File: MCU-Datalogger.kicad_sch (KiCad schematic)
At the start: 0 parts

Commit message: Added symbols into the schematics
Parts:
- added BT1: Battery, symbol Device:Battery
- added C1, C2, C3, C4: C, symbol Device:C
- added C5: C_Polarized, symbol Device:C_Polarized
- added D1, D2: LED, symbol Device:LED
- added H1, H2, H3, H4: MountingHole, symbol Mechanical:MountingHole
- added R1, R2, R3, R4, R5, R6, R7: R, symbol Device:R
- added U1, U2: 24LC1025, symbol Memory_EEPROM:24LC1025
- added U3: DS1337S_, DS1337S_:SOIC127P600X175-8N, symbol DS1337S:DS1337S_
- added U4: ATMEGA328PB-AU, ATMEGA328PB-AU:QFP80P900X900X120-32N, symbol ATMEGA328P-AU:ATMEGA328PB-AU
- added Y1, Y2: Crystal, symbol Device:Crystal
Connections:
- new net GND: U4.21 (GND), U4.5 (GND)
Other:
- added sheet Connectors (Connectors.kicad_sch)
- company: (none) -> Foxhill Labs
- title: (none) -> ${project_name}

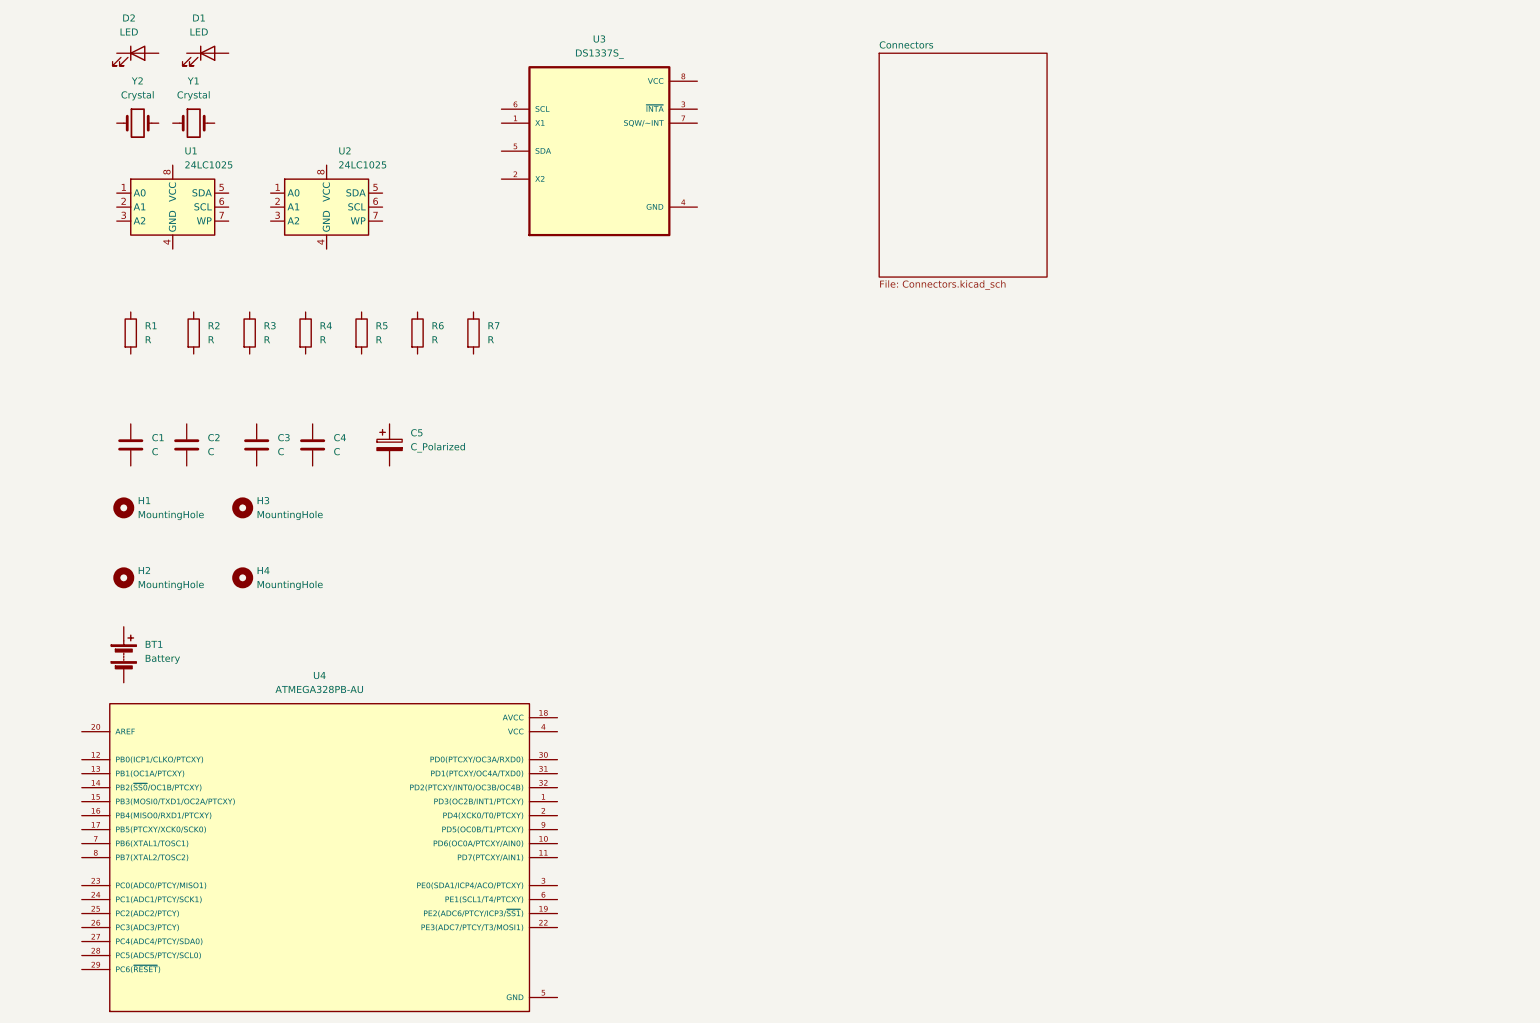
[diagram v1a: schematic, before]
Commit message: Wiring Completion
Wiring completed and the symbols have been rearranged, the footprints were added for all of the symbols. Connector hierarchical sheet added to the project.
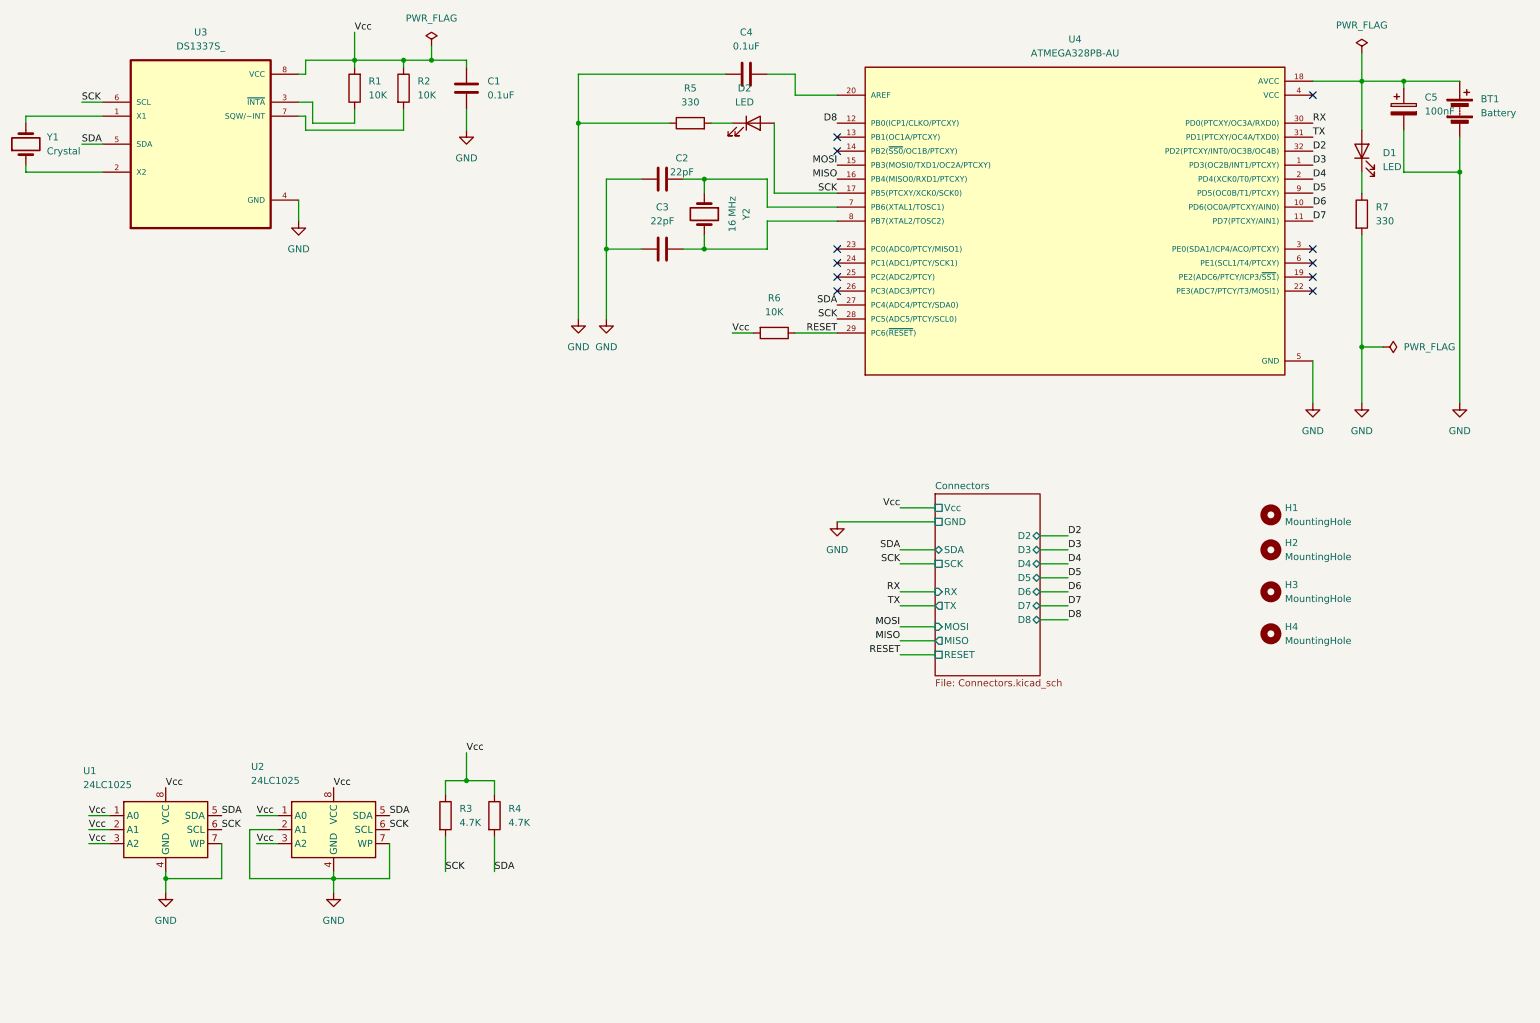
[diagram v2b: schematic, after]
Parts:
- BT1: footprint (none) -> Connector_PinHeader_2.54mm:PinHeader_1x02_P2.54mm_Vertical
- C1, C4: value C -> 0.1uF; footprint (none) -> Capacitor_SMD:C_0805_2012Metric
- C2, C3: value C -> 22pF; footprint (none) -> Capacitor_SMD:C_0805_2012Metric
- C5: value C_Polarized -> 100nF; footprint (none) -> Capacitor_SMD:C_0805_2012Metric
- D1, D2: footprint (none) -> LED_SMD:LED_0805_2012Metric
- H1, H2, H3, H4: footprint (none) -> MountingHole:MountingHole_2.1mm
- R1, R2, R6: value R -> 10K; footprint (none) -> Resistor_SMD:R_0805_2012Metric
- R3, R4: value R -> 4.7K; footprint (none) -> Resistor_SMD:R_0805_2012Metric
- R5, R7: value R -> 330; footprint (none) -> Resistor_SMD:R_0805_2012Metric
- U1, U2: footprint (none) -> Package_SO:SOIC-8_5.3x5.3mm_P1.27mm
- U3: footprint DS1337S_:SOIC127P600X175-8N -> DS1337S:SOIC127P600X175-8N
- U4: footprint ATMEGA328PB-AU:QFP80P900X900X120-32N -> ATMEGA328P-AU:QFP80P900X900X120-32N
- Y1: footprint (none) -> Crystal:Crystal_SMD_5032-2Pin_5.0x3.2mm_HandSoldering
- Y2: value Crystal -> 16 MHz; footprint (none) -> Crystal:Crystal_SMD_5032-2Pin_5.0x3.2mm_HandSoldering
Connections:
- net GND: now also BT1.2 (-), C1.2, C2.1, C3.1, C4.1, C5.2, R5.1, R7.2, U1.4 (GND), U1.7 (WP), U2.2 (A1), U2.4 (GND), U2.7 (WP), U3.4 (GND)
- net at Y1.1: now also U3.2 (X2)
- net at Y1.2: now also U3.1 (X1)
- net Vcc: now reaches R2.1
- net Vcc: now also C1.1, R1.2, R3.1, R4.1, R6.2, U1.1 (A0), U1.2 (A1), U1.3 (A2), U1.8 (VCC), U2.1 (A0), U2.3 (A2), U2.8 (VCC), U3.8 (VCC)
- net at R2.2: now also U3.7 (SQW/~INT)
- net at R7.1: now also D1.1 (K)
- net SDA: now reaches U1.5 (SDA)
- net SDA: now also R4.2, U2.5 (SDA), U3.5 (SDA), U4.27 (PC4(ADC4/PTCY/SDA0))
- net SCK: now reaches U1.6 (SCL)
- net SCK: now also D2.2 (A), R3.2, U2.6 (SCL), U3.6 (SCL), U4.17 (PB5(PTCXY/XCK0/SCK0)), U4.28 (PC5(ADC5/PTCY/SCL0))
- net at C2.2: now also U4.7 (PB6(XTAL1/TOSC1)), Y2.1
- net at D1.2 (A): now also BT1.1 (+), C5.1, U4.18 (AVCC)
- net at U3.3 (~{INTA}): now also R1.1
- net at C3.2: now also U4.8 (PB7(XTAL2/TOSC2)), Y2.2
- net D3: now reaches U4.1 (PD3(OC2B/INT1/PTCXY))
- net D6: now reaches U4.10 (PD6(OC0A/PTCXY/AIN0))
- net D7: now reaches U4.11 (PD7(PTCXY/AIN1))
- net D8: now reaches U4.12 (PB0(ICP1/CLKO/PTCXY))
- net MOSI: now reaches U4.15 (PB3(MOSI0/TXD1/OC2A/PTCXY))
- net MISO: now reaches U4.16 (PB4(MISO0/RXD1/PTCXY))
- net D4: now reaches U4.2 (PD4(XCK0/T0/PTCXY))
- net at U4.20 (AREF): now also C4.2
- net RESET: now reaches U4.29 (PC6(~{RESET}))
- net RESET: now also R6.1
- net RX: now reaches U4.30 (PD0(PTCXY/OC3A/RXD0))
- net TX: now reaches U4.31 (PD1(PTCXY/OC4A/TXD0))
- net D2: now reaches U4.32 (PD2(PTCXY/INT0/OC3B/OC4B))
- net D5: now reaches U4.9 (PD5(OC0B/T1/PTCXY))
- net at D2.1 (K): now also R5.2
- no-connect marks 0 -> 11
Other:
- sheet Connectors ports: added D2, D3, D4, D5, D6, D7, D8, GND, MISO, MOSI, RESET, RX, SCK, SDA, TX, Vcc; removed none
- moved on the sheet: BT1, C1, C2, C3, C4, C5, D1, D2, H1, H2, H3, H4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

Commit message: Comments
Completed the comments for the schematics
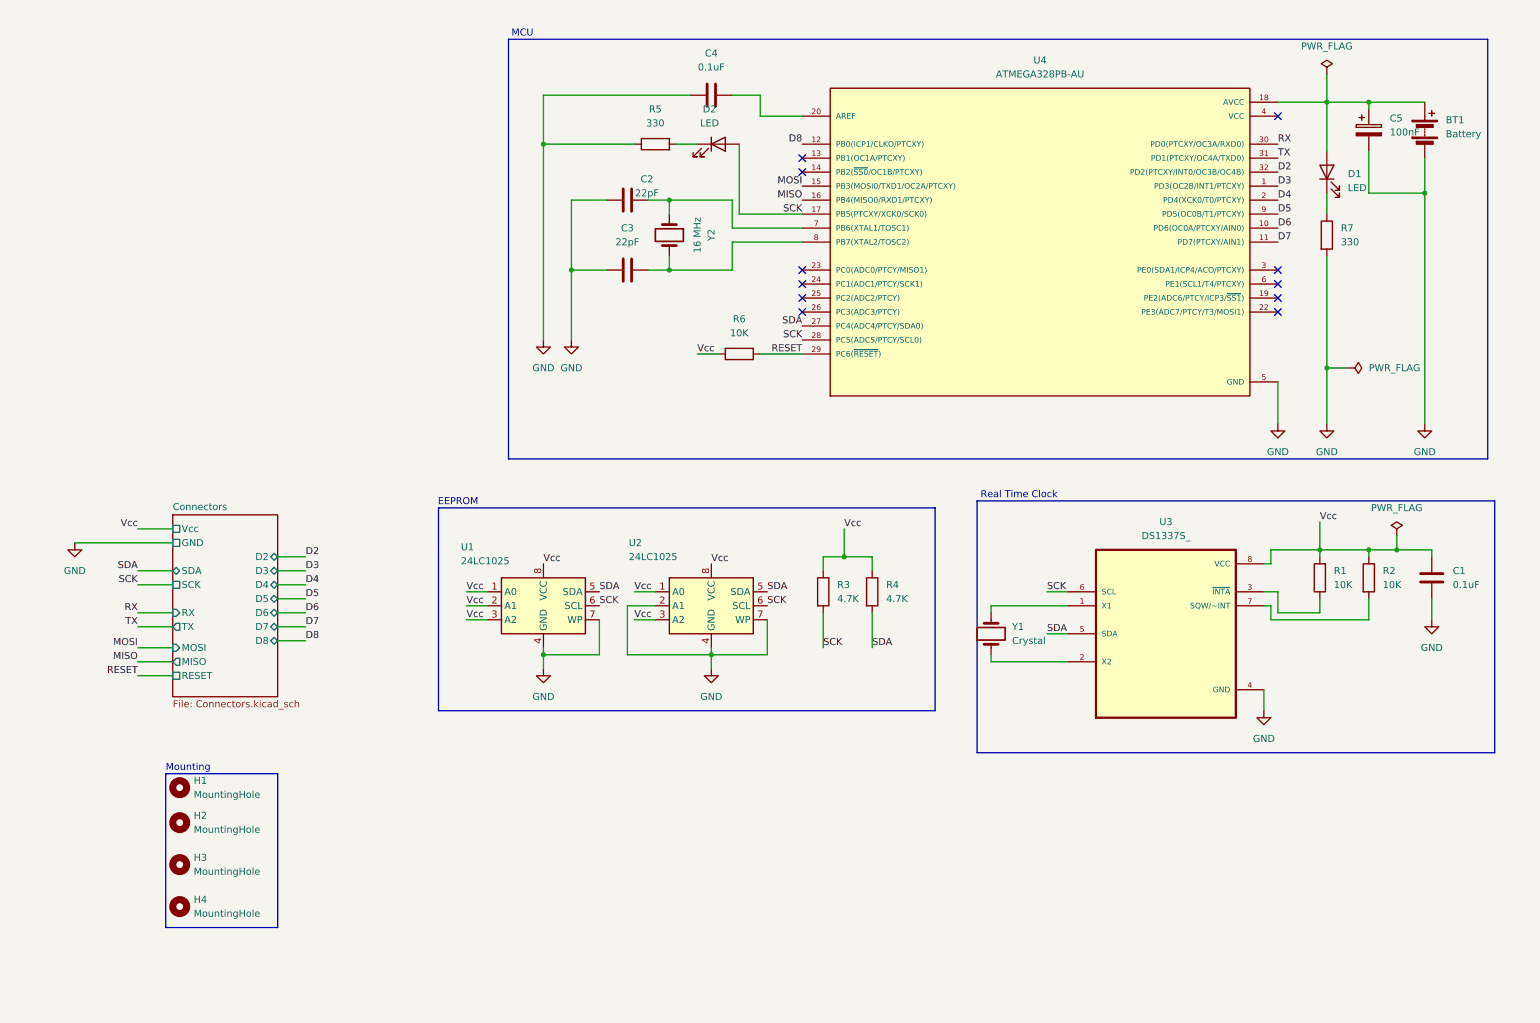
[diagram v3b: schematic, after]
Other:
- note added: "EEPROM"
- note added: "MCU"
- note added: "Mounting"
- note added: "Real Time Clock"
- moved on the sheet: BT1, C1, C2, C3, C4, C5, D1, D2, H1, H2, H3, H4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
